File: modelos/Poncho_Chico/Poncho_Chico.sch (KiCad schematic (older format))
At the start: 3 parts, among them P1 CONN_5, P2 CONN_4

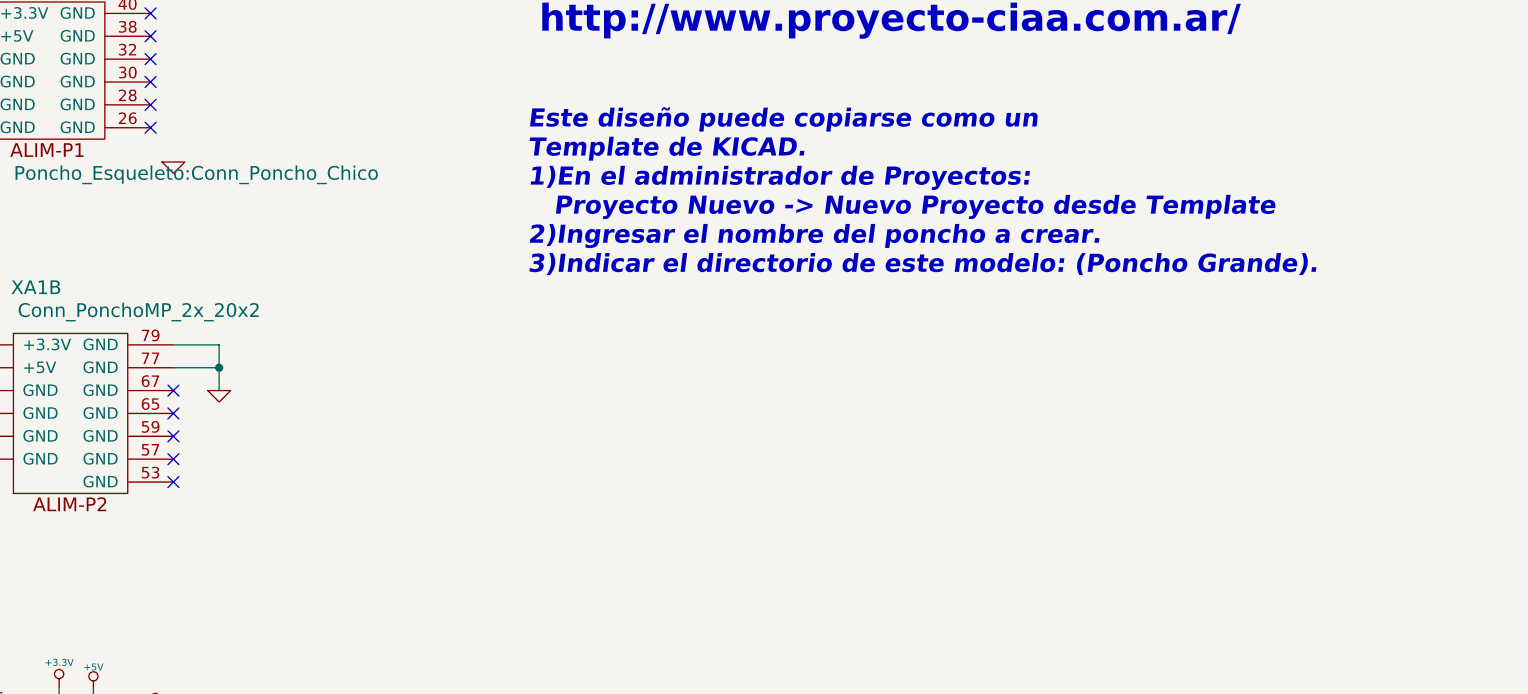
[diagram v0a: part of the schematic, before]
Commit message: * Agrego textos instructivos en esquema y PCB.
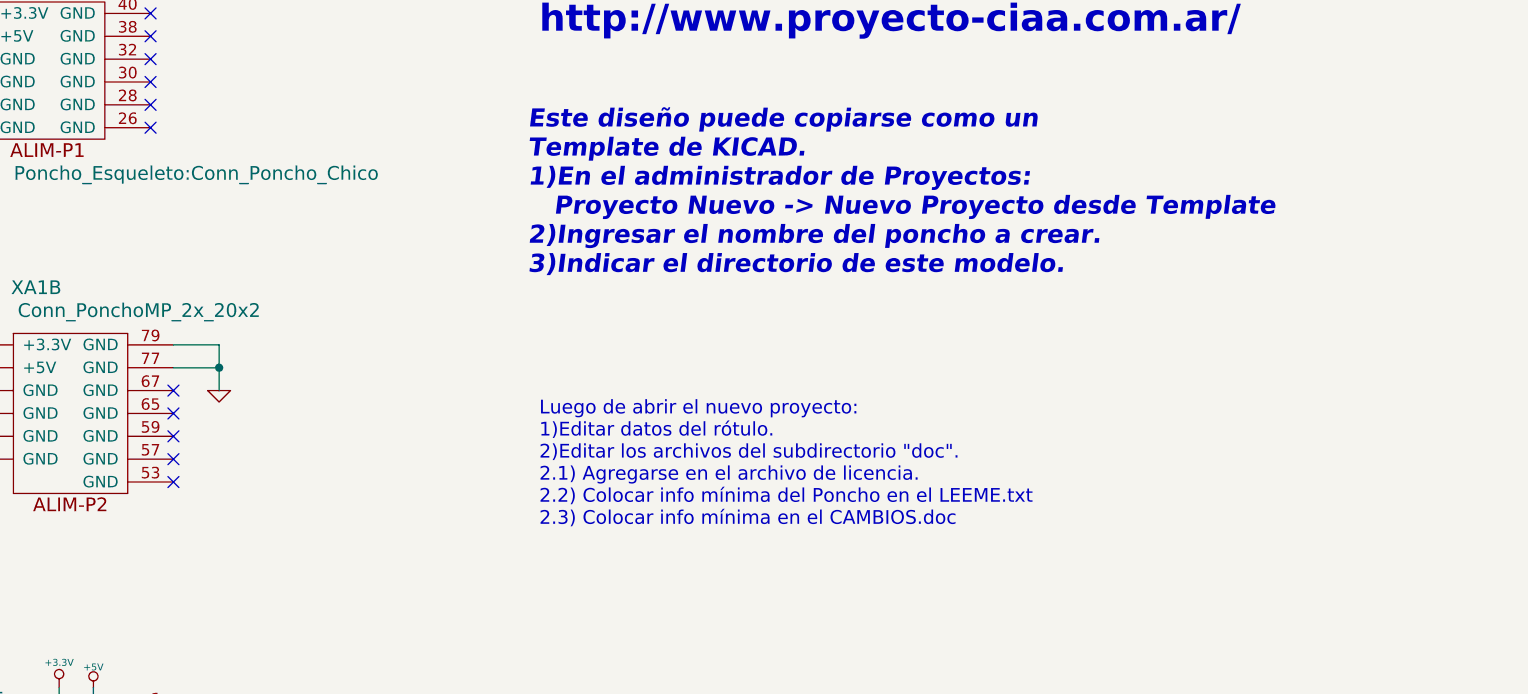
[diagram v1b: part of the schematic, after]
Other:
- note added: "Este diseño puede copiarse como un \nTemplate de KICAD. \n1)En el administrador de Proyectos: \n Proyecto Nuevo -> Nuevo Proyecto desde Template\n2)Ingresar el nombre del poncho a crear.\n3)Indicar el directorio de este modelo."
- note added: "Luego de abrir el nuevo proyecto:\n1)Editar datos del rótulo.\n2)Editar los archivos del subdirectorio "doc".\n2.1) Agregarse en el archivo de licencia.\n2.2) Colocar info mínima del Poncho en el LEEME.txt\n2.3) Colocar info mínima en el CAMBIOS.doc"
- note removed: "Este diseño puede copiarse como un \nTemplate de KICAD. \n1)En el administrador de Proyectos: \n Proyecto Nuevo -> Nuevo Proyecto desde Template\n2)Ingresar el nombre del poncho a crear.\n3)Indicar el directorio de este modelo: (Poncho Grande)."
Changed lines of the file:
@@
 EESchema Schematic File Version 2
 LIBS:Misc_Poncho_Grande
-LIBS:conn
-LIBS:diode
-LIBS:interface
-LIBS:maxim
-LIBS:onsemi
-LIBS:relays
-LIBS:transistors
 LIBS:Poncho_Esqueleto
 LIBS:Poncho_Chico-cache
@@
 Comment1 "https://github.com/ciaa/Ponchos/tree/master/modelos/doc"
 Comment2 "Autores y Licencia del template"
-Comment3 ""
+Comment3 "CÓDIGO PONCHO:"
 Comment4 ""
 $EndDescr
@@
 $EndComp
 Text Notes 6950 2850 0    79   Italic 16
-Este diseño puede copiarse como un \nTemplate de KICAD. \n1)En el administrador de Proyectos:  \n   Proyecto Nuevo -> Nuevo Proyecto desde Template\n2)Ingresar el nombre del poncho a crear.\n3)Indicar el directorio de este modelo: (Poncho Grande).
+Este diseño puede copiarse como un \nTemplate de KICAD. \n1)En el administrador de Proyectos:  \n   Proyecto Nuevo -> Nuevo Proyecto desde Template\n2)Ingresar el nombre del poncho a crear.\n3)Indicar el directorio de este modelo.
 Text Notes 7000 1800 0    118  ~ 24
 http://www.proyecto-ciaa.com.ar/
@@
 $Comp
 L GND #PWR011
-U 1 1 560EE313
-P 5400 2350
-F 0 "#PWR011" H 5400 2350 30  0001 C CNN
-F 1 "GND" H 5400 2280 30  0001 C CNN
-F 2 "" H 5400 2350 60  0000 C CNN
-F 3 "" H 5400 2350 60  0000 C CNN
-	1    5400 2350
-	1    0    0    -1
-$EndComp
-$Comp
-L GND #PWR012
 U 1 1 560EE345
 P 5600 3350
-F 0 "#PWR012" H 5600 3350 30  0001 C CNN
+F 0 "#PWR011" H 5600 3350 30  0001 C CNN
 F 1 "GND" H 5600 3280 30  0001 C CNN
 F 2 "" H 5600 3350 60  0000 C CNN
@@
 NoConn ~ 4400 1900
 $Comp
-L +5VP #PWR013
+L +5VP #PWR012
 U 1 1 560EE7D3
 P 4150 3150
-F 0 "#PWR013" H 4150 3240 20  0001 C CNN
+F 0 "#PWR012" H 4150 3240 20  0001 C CNN
 F 1 "+5VP" H 4150 3240 30  0000 C CNN
 F 2 "" H 4150 3150 60  0000 C CNN
@@
 	4150 3250 4150 3150
 $Comp
-L PWR_FLAG #FLG014
+L PWR_FLAG #FLG013
 U 1 1 560EE826
 P 3900 3250
-F 0 "#FLG014" H 3900 3345 30  0001 C CNN
+F 0 "#FLG013" H 3900 3345 30  0001 C CNN
 F 1 "PWR_FLAG" H 3900 3430 30  0000 C CNN
 F 2 "" H 3900 3250 60  0000 C CNN
@@
 Connection ~ 4150 3250
 $Comp
-L +5VP #PWR015
+L +5VP #PWR014
 U 1 1 560EE8BF
 P 5300 6100
-F 0 "#PWR015" H 5300 6190 20  0001 C CNN
+F 0 "#PWR014" H 5300 6190 20  0001 C CNN
 F 1 "+5VP" H 5300 6190 30  0000 C CNN
 F 2 "" H 5300 6100 60  0000 C CNN
@@
 NoConn ~ 4400 2100
 NoConn ~ 4400 2000
+Text Notes 7000 3950 0    60   ~ 0
+Luego de abrir el nuevo proyecto:\n1)Editar datos del rótulo.\n2)Editar los archivos del subdirectorio "doc".\n2.1) Agregarse en el archivo de licencia.\n2.2) Colocar info mínima del Poncho en el LEEME.txt\n2.3) Colocar info mínima en el CAMBIOS.doc
 $EndSCHEMATC
